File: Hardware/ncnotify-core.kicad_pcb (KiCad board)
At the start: 4 copper layers, 43.4 x 21 mm, 44 parts, among them J1 BNC5-J-P-GN-RA-BH2D, J2 Conn_ARM_JTAG_SWD_10, J3 USB4110-GF-A, Q1 NX3008NBKS, SW1 SW_Push, SW2 SW_Push, U1 STM32L422CBT6, U2 TLV71333PDBV, U3 USBLC6-2SC6, U4 USBLC6-2SC6, Y1 Q13FC1350000400

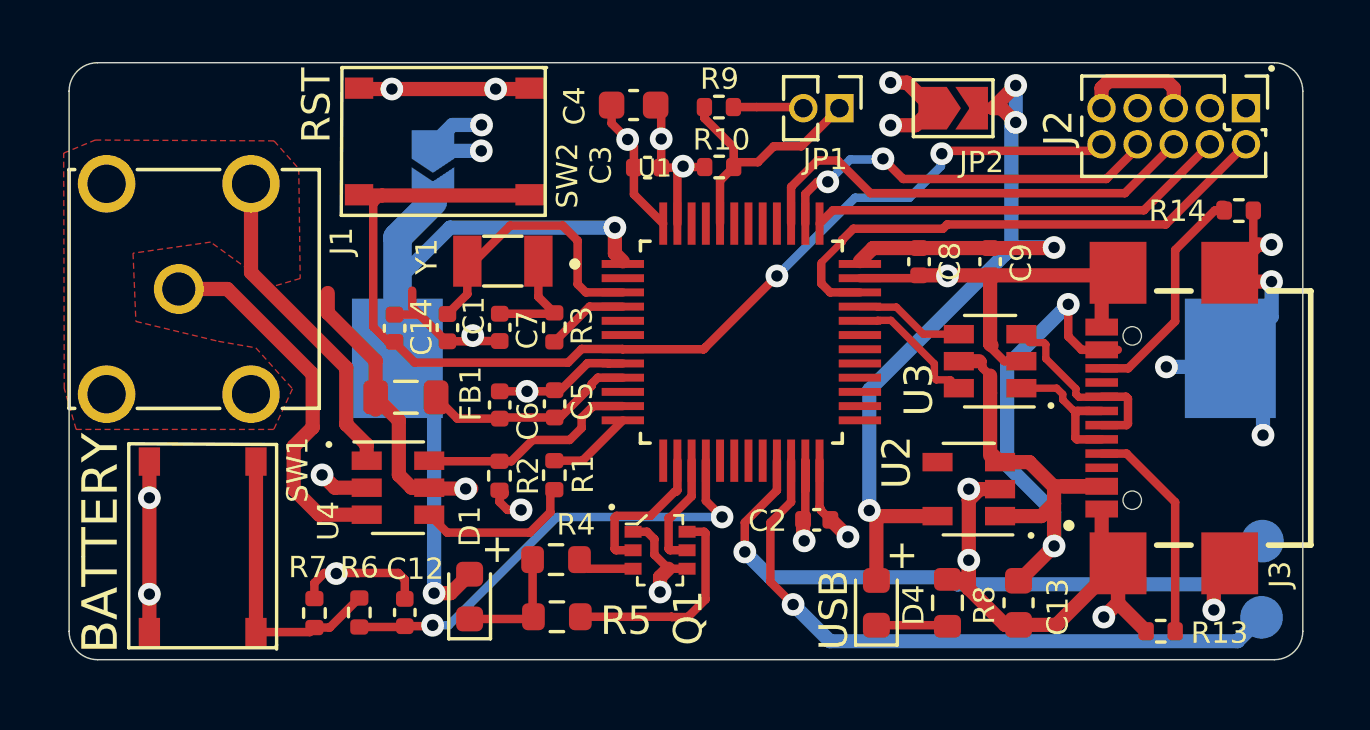
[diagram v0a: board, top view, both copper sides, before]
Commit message: Change batt status leds; add spi/i2c test points
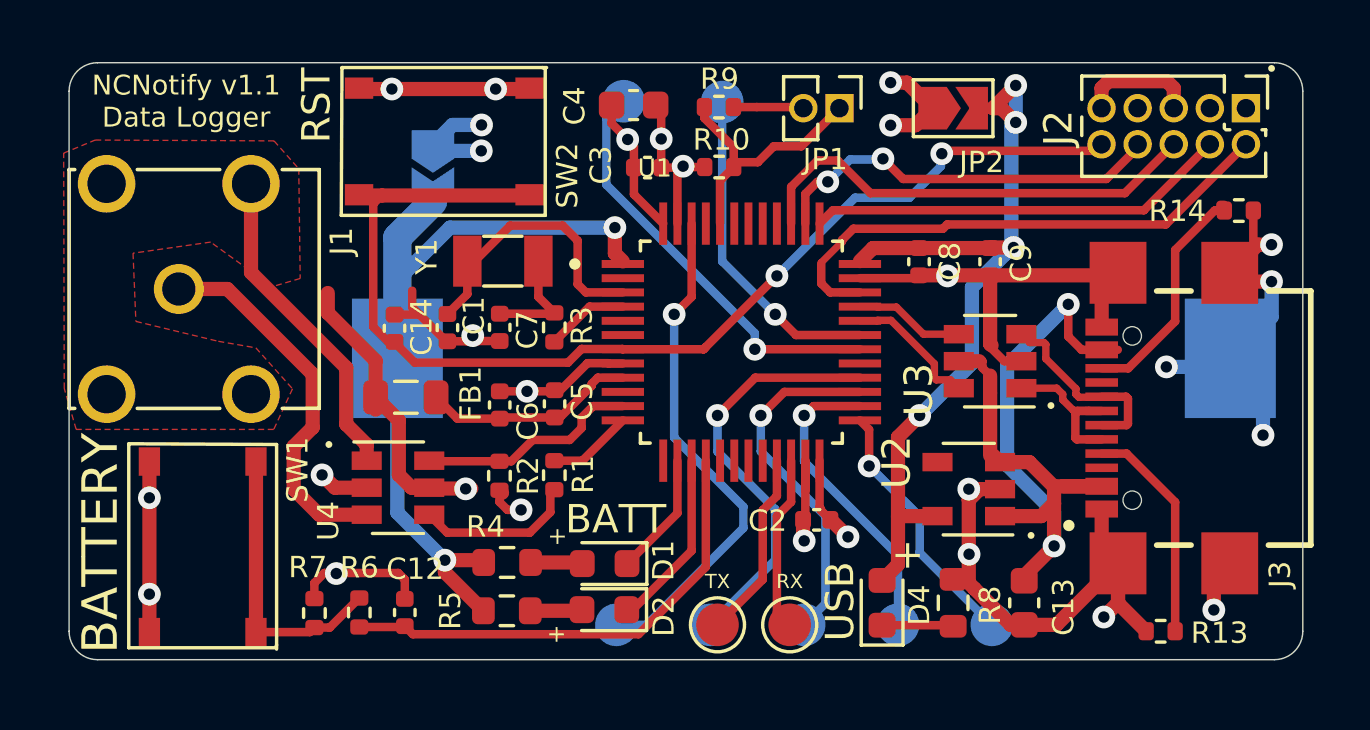
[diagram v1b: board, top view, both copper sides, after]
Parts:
- removed Q1: NX3008NBKS, digikey-footprints:SOT-363
- added CIPO: TestPoint, libs:TestPoint_Pad_D1.5mm_No_Ctrd, B.Cu at (235.5, -30.2)
- added COPI: TestPoint, libs:TestPoint_Pad_D1.5mm_No_Ctrd, B.Cu at (232.2, -30.2)
- added CS_0: TestPoint, libs:TestPoint_Pad_D1.5mm_No_Ctrd, B.Cu at (242.1, -30.2)
- added CS_1: TestPoint, libs:TestPoint_Pad_D1.5mm_No_Ctrd, B.Cu at (228.9, -30.2)
- added D2: Vf ~~ 2.1 Green, LED_SMD:LED_0603_1608Metric, F.Cu at (228.4, -30.8)
- added SCK: TestPoint, libs:TestPoint_Pad_D1.5mm_No_Ctrd, B.Cu at (238.8, -30.2)
- added TP7: TestPoint, libs:TestPoint_Pad_D1.5mm_No_Ctrd, B.Cu at (232.6, -48.6)
- added TP8: TestPoint, libs:TestPoint_Pad_D1.5mm_No_Ctrd, B.Cu at (229.1, -48.6)
- D1: value Vf ~ 2.1 -> Vf ~~ 2.0 Red
- R4: value 15 -> 24
- TP1, TP2: footprint TestPoint:TestPoint_Pad_D1.5mm -> libs:TestPoint_Pad_D1.5mm_No_Ctrd; moved to F.Cu
- moved TP2 19.4 mm to (232.4, -30.2), turned to 90 degrees
- moved TP1 16.6 mm to (234.9, -30.2), turned to 270 degrees
- moved D1 4.89 mm to (228.4, -32.4), turned to 180 degrees
- moved R5 1.77 mm to (225.0, -30.7)
- moved R4 1.72 mm to (225.0, -32.4)
- moved C13 0.20 mm to (243.2, -31.0)
- moved D4 0.20 mm to (238.2, -31.0)
- moved R8 0.20 mm to (240.7, -31.0)
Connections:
- D1 pad 1: Net-(D1-Pad1) -> LED_BATT_YEL
- D1 pad 2: VBAT -> Net-(D1-Pad2)
- R4 pad 1: Net-(D1-Pad1) -> VBAT
- R4 pad 2: Net-(Q1-Pad3) -> Net-(D1-Pad2)
- R5 pad 1: Net-(D1-Pad1) -> VBAT
- U1 pad 14: LED_LOW_V -> LED_BATT_YEL
- U1 pad 15: LED_HI_V -> LED_BATT_GRN
- U1 pad 46: Net-(U1-Pad46) -> SPI2_SS_1
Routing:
- net SPI2_SS_1: track 0.00 -> 17.8 mm, vias 0 -> 1
- net USART3_RX: track 23.1 -> 6.17 mm, vias 1 -> 0
- net USART3_TX: track 23.0 -> 6.64 mm, vias 1 -> 0
- net I2C1_SCL: track 0.00 -> 14.8 mm, vias 0 -> 1
- net SPI2_MOSI: track 0.00 -> 14.7 mm, vias 0 -> 1
- net SPI2_MISO: track 0.00 -> 12.4 mm, vias 0 -> 1
- net I2C1_SDA: track 0.00 -> 11.5 mm, vias 0 -> 1
- net SPI2_SCK: track 0.00 -> 10.8 mm, vias 0 -> 1
- net SPI2_SS_0: track 0.00 -> 9.12 mm, vias 0 -> 1
- net LED_BATT_GRN: track 0.00 -> 6.38 mm
- net Net-(D2-Pad2): track 7.67 -> 1.83 mm
- net LED_LOW_V: track 5.42 -> 0.00 mm
- net GND: track 99.6 -> 94.8 mm, vias 20 -> 19
- net LED_BATT_YEL: track 0.00 -> 4.35 mm
- net VBUS: track 33.5 -> 29.2 mm
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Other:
- board text added: "BATT"
- board text added: "NCNotify Data Logger Bowen Shaner"
- board text added: "NCNotify v1.1 Data Logger"
- board text removed: "v1.1 NCNotify Data Logger Bowen Shaner"

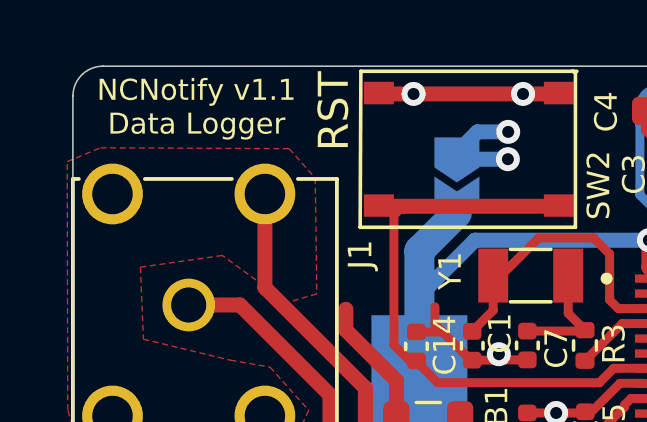
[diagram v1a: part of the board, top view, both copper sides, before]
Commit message: swap usb port and reroute
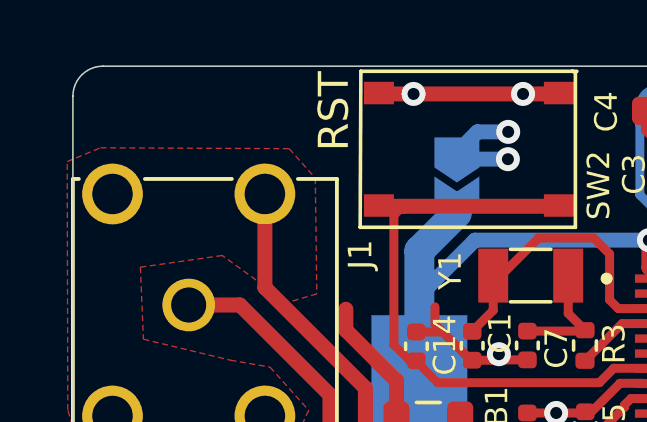
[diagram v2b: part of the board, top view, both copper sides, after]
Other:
- board text removed: "NCNotify Data Logger Bowen Shaner"
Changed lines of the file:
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@@
   (general
     (thickness 1.6)
-    (drawings 25)
+    (drawings 24)
     (tracks 490)
     (zones 0)
@@
     (34 B.Paste user)
     (35 F.Paste user)
-    (36 B.SilkS user hide)
-    (37 F.SilkS user hide)
+    (36 B.SilkS user)
+    (37 F.SilkS user)
     (38 B.Mask user)
     (39 F.Mask user)
@@
     (47 F.CrtYd user)
     (48 B.Fab user)
-    (49 F.Fab user hide)
+    (49 F.Fab user)
   )
   (setup
-    (last_trace_width 0.5)
+    (last_trace_width 0.25)
     (user_trace_width 0.3)
     (user_trace_width 0.5)
@@
       (effects (font (size 1 1) (thickness 0.15)) (justify mirror))
     )
+    (fp_circle (center 0 0) (end 0 -0.95) (layer B.SilkS) (width 0.12))
     (fp_text user %R (at 0 1.65 180) (layer B.Fab)
       (effects (font (size 1 1) (thickness 0.15)) (justify mirror))
     )
-    (fp_circle (center 0 0) (end 0 -0.95) (layer B.SilkS) (width 0.12))
     (pad 1 smd circle (at 0 0 180) (size 1.5 1.5) (layers B.Cu B.Mask)
       (net 21 SPI2_SS_0))
@@
       (effects (font (size 1 1) (thickness 0.15)) (justify mirror))
     )
+    (fp_circle (center 0 0) (end 0 -0.95) (layer B.SilkS) (width 0.12))
     (fp_text user %R (at 0 1.65 180) (layer B.Fab)
       (effects (font (size 1 1) (thickness 0.15)) (justify mirror))
     )
-    (fp_circle (center 0 0) (end 0 -0.95) (layer B.SilkS) (width 0.12))
     (pad 1 smd circle (at 0 0 180) (size 1.5 1.5) (layers B.Cu B.Mask)
       (net 61 SPI2_SS_1))
@@
       (effects (font (size 1 1) (thickness 0.15)) (justify mirror))
     )
+    (fp_circle (center 0 0) (end 0 -0.95) (layer B.SilkS) (width 0.12))
     (fp_text user %R (at 0 1.65) (layer B.Fab)
       (effects (font (size 1 1) (thickness 0.15)) (justify mirror))
     )
-    (fp_circle (center 0 0) (end 0 -0.95) (layer B.SilkS) (width 0.12))
     (pad 1 smd circle (at 0 0 180) (size 1.5 1.5) (layers B.Cu B.Mask)
       (net 17 SPI2_SCK))
@@
       (effects (font (size 1 1) (thickness 0.15)) (justify mirror))
     )
+    (fp_circle (center 0 0) (end 0 -0.95) (layer B.SilkS) (width 0.12))
     (fp_text user %R (at 0 1.65) (layer B.Fab)
       (effects (font (size 1 1) (thickness 0.15)) (justify mirror))
     )
-    (fp_circle (center 0 0) (end 0 -0.95) (layer B.SilkS) (width 0.12))
     (pad 1 smd circle (at 0 0) (size 1.5 1.5) (layers B.Cu B.Mask)
       (net 16 I2C1_SDA))
@@
       (effects (font (size 1 1) (thickness 0.15)) (justify mirror))
     )
+    (fp_circle (center 0 0) (end 0 -0.95) (layer B.SilkS) (width 0.12))
     (fp_text user %R (at 0 1.65) (layer B.Fab)
       (effects (font (size 1 1) (thickness 0.15)) (justify mirror))
     )
-    (fp_circle (center 0 0) (end 0 -0.95) (layer B.SilkS) (width 0.12))
     (pad 1 smd circle (at 0 0 180) (size 1.5 1.5) (layers B.Cu B.Mask)
       (net 19 SPI2_MISO))
@@
       (effects (font (size 1 1) (thickness 0.15)) (justify mirror))
     )
+    (fp_circle (center 0 0) (end 0 -0.95) (layer B.SilkS) (width 0.12))
     (fp_text user %R (at 0 1.65) (layer B.Fab)
       (effects (font (size 1 1) (thickness 0.15)) (justify mirror))
     )
-    (fp_circle (center 0 0) (end 0 -0.95) (layer B.SilkS) (width 0.12))
     (pad 1 smd circle (at 0 0 180) (size 1.5 1.5) (layers B.Cu B.Mask)
       (net 20 SPI2_MOSI))
@@
       (effects (font (size 1 1) (thickness 0.15)) (justify mirror))
     )
+    (fp_circle (center 0 0) (end 0 -0.95) (layer B.SilkS) (width 0.12))
     (fp_text user %R (at 0 1.65) (layer B.Fab)
       (effects (font (size 1 1) (thickness 0.15)) (justify mirror))
     )
-    (fp_circle (center 0 0) (end 0 -0.95) (layer B.SilkS) (width 0.12))
     (pad 1 smd circle (at 0 0) (size 1.5 1.5) (layers B.Cu B.Mask)
       (net 18 I2C1_SCL))
@@
       (effects (font (size 1 1) (thickness 0.15)))
     )
+    (fp_circle (center 0 0) (end 0 0.95) (layer F.SilkS) (width 0.12))
     (fp_text user %R (at 0 -1.65 90) (layer F.Fab) hide
       (effects (font (size 1 1) (thickness 0.15)))
     )
-    (fp_circle (center 0 0) (end 0 0.95) (layer F.SilkS) (width 0.12))
     (pad 1 smd circle (at 0 0 90) (size 1.5 1.5) (layers F.Cu F.Mask)
       (net 55 USART3_TX))
@@
       (effects (font (size 1 1) (thickness 0.15)))
     )
+    (fp_circle (center 0 0) (end 0 0.95) (layer F.SilkS) (width 0.12))
     (fp_text user %R (at 0 -1.65 90) (layer F.Fab) hide
       (effects (font (size 1 1) (thickness 0.15)))
     )
-    (fp_circle (center 0 0) (end 0 0.95) (layer F.SilkS) (width 0.12))
     (pad 1 smd circle (at 0 0 270) (size 1.5 1.5) (layers F.Cu F.Mask)
       (net 54 USART3_RX))
@@
     (fp_text value BNC5-J-P-GN-RA-BH2D (at 8.82138 4.826205 90) (layer F.Fab)
       (effects (font (size 0.788417 0.788417) (thickness 0.015)))
-    )
-    (fp_text user PCB~EDGE (at -1.6012 3.75282 90) (layer F.Fab)
-      (effects (font (size 0.393997 0.393997) (thickness 0.015)))
     )
     (fp_line (start 4.2 3.86) (end -4.2 3.86) (layer F.Fab) (width 0.127))
@@
     (fp_line (start 5.45 24.31) (end 5.45 3.74) (layer F.CrtYd) (width 0.05))
     (fp_line (start 5.45 3.74) (end 4.96 3.74) (layer F.CrtYd) (width 0.05))
+    (fp_text user PCB~EDGE (at -1.6012 3.75282 90) (layer F.Fab)
+      (effects (font (size 0.393997 0.393997) (thickness 0.015)))
+    )
     (pad 1 thru_hole circle (at 0 0 270) (size 1.755 1.755) (drill 1.17) (layers *.Cu *.Mask)
       (net 13 S+))
@@
       (effects (font (size 1.000094 1.000094) (thickness 0.015)) (justify mirror))
     )
-    (fp_arc (start 0 0) (end 4.401753 8.99914) (angle 52.11815805) (layer B.CrtYd) (width 0.12))
-    (fp_arc (start 0 0) (end -4.399999 -8.999999) (angle 52.10699062) (layer B.CrtYd) (width 0.12))
     (fp_line (start -14.3 -3.5) (end -14.3 3.5) (layer B.Fab) (width 0.127))
     (fp_line (start -14.3 3.5) (end -10.645 3.5) (layer B.Fab) (width 0.127))
@@
     (fp_line (start -11.1 4) (end -8 9) (layer B.CrtYd) (width 0.12))
     (fp_line (start -8 9) (end -4.399999 8.999998) (layer B.CrtYd) (width 0.12))
+    (fp_arc (start 0 0) (end 4.401753 8.99914) (angle 52.11815805) (layer B.CrtYd) (width 0.12))
+    (fp_arc (start 0 0) (end -4.399999 -8.999999) (angle 52.10699062) (layer B.CrtYd) (width 0.12))
     (pad + smd rect (at -14.65 0) (size 3.2 4.2) (layers B.Cu B.Paste B.Mask)
       (net 10 VBAT))
@@
     (fp_text value "Vf ~~ 2.1 Green" (at 0 1.43) (layer F.Fab)
       (effects (font (size 1 1) (thickness 0.15)))
-    )
-    (fp_text user %R (at 0 0) (layer F.Fab)
-      (effects (font (size 0.4 0.4) (thickness 0.06)))
     )
     (fp_line (start 0.8 -0.4) (end -0.5 -0.4) (layer F.Fab) (width 0.1))
@@
     (fp_line (start 1.48 -0.73) (end 1.48 0.73) (layer F.CrtYd) (width 0.05))
     (fp_line (start 1.48 0.73) (end -1.48 0.73) (layer F.CrtYd) (width 0.05))
+    (fp_text user %R (at 0 0) (layer F.Fab)
+      (effects (font (size 0.4 0.4) (thickness 0.06)))
+    )
     (pad 2 smd roundrect (at 0.7875 0 180) (size 0.875 0.95) (layers F.Cu F.Paste F.Mask) (roundrect_rratio 0.25)
       (net 59 "Net-(D2-Pad2)"))
@@
     (effects (font (size 0.5 0.5) (thickness 0.125)))
   )
-  (gr_text "NCNotify v1.1\nData Logger" (at 213.72 -48.64) (layer F.SilkS)
-    (effects (font (size 0.7 0.7) (thickness 0.15)))
+  (gr_text "NCNotify v1.1\nData Logger" (at 214.122 -33.02) (layer B.SilkS)
+    (effects (font (size 0.7 0.7) (thickness 0.15)) (justify mirror))
   )
   (gr_circle (center 251.9 -49.8) (end 251.96 -49.8) (layer F.SilkS) (width 0.12))
@@
   )
   (gr_text JLCJLCJLCJLC (at 235.7 -39.6) (layer B.SilkS)
-    (effects (font (size 1 1) (thickness 0.15)) (justify mirror))
-  )
-  (gr_text "NCNotify Data Logger\n   Bowen Shaner" (at 217.8 -32.5) (layer B.SilkS)
     (effects (font (size 1 1) (thickness 0.15)) (justify mirror))
   )
@@
   (segment (start 243.2 -30.225) (end 242.725 -30.225) (width 0.5) (layer F.Cu) (net 1))
   (segment (start 242.725 -30.225) (end 241.45 -31.5) (width 0.5) (layer F.Cu) (net 1))
-  (via (at 234.442 -41.148) (size 0.8) (drill 0.4) (layers F.Cu B.Cu) (net 16))
   (segment (start 223.61 -41.86) (end 222.91 -41.16) (width 0.3) (layer F.Cu) (net 2))
   (segment (start 223.61 -43.02) (end 223.61 -41.86) (width 0.3) (layer F.Cu) (net 2))
@@
   (segment (start 240.6625 -30.2125) (end 240.7 -30.175) (width 0.3) (layer F.Cu) (net 15))
   (segment (start 238.2 -30.2125) (end 240.6625 -30.2125) (width 0.3) (layer F.Cu) (net 15))
+  (via (at 234.442 -41.148) (size 0.8) (drill 0.4) (layers F.Cu B.Cu) (net 16))
   (segment (start 235.17 -40.42) (end 234.442 -41.148) (width 0.3) (layer F.Cu) (net 16))
   (segment (start 237.42 -40.42) (end 235.17 -40.42) (width 0.3) (layer F.Cu) (net 16))
